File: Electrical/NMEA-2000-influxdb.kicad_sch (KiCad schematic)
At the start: 6 parts, among them U1 LM7805_TO220, U2 SN65HVD230-Module, U3 RTC-Module

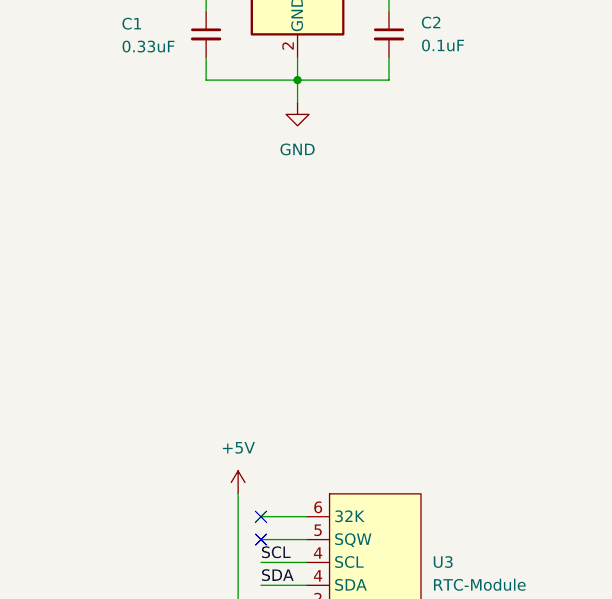
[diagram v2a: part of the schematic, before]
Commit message: Added BMP280-Module
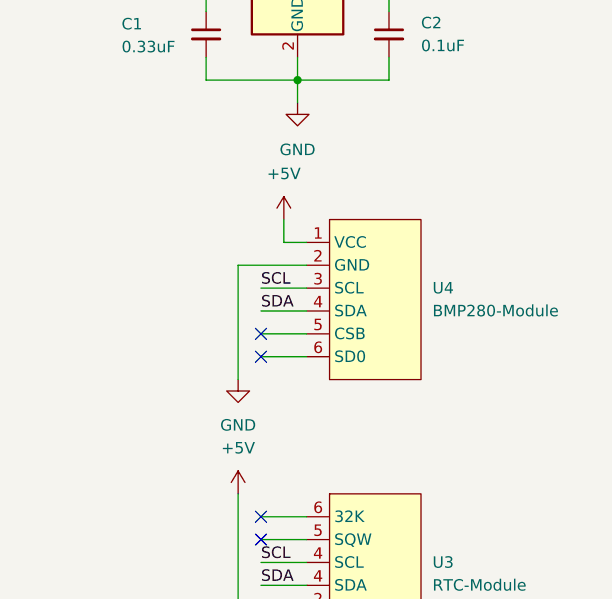
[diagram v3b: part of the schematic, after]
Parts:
- added U4: BMP280-Module, symbol BMP280-Module:BMP280-Module
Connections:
- net +5V: now also U4.1 (VCC)
- net GND: now also U4.2 (GND)
- net SCL: now also U4.3 (SCL)
- net SDA: now also U4.4 (SDA)
- no-connect marks 2 -> 4
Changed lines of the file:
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@@
   )
   (no_connect (at 222.25 99.06))
+  (no_connect (at 222.25 81.28))
   (no_connect (at 222.25 101.6))
+  (no_connect (at 222.25 78.74))
   (wire (pts (xy 222.25 99.06) (xy 227.33 99.06))
     (stroke (width 0) (type default))
   )
+  (wire (pts (xy 222.25 81.28) (xy 227.33 81.28))
+    (stroke (width 0) (type default))
+  )
+  (wire (pts (xy 222.25 76.2) (xy 227.33 76.2))
+    (stroke (width 0) (type default))
+  )
   (wire (pts (xy 222.25 109.22) (xy 222.25 114.3))
     (stroke (width 0) (type default))
@@
     (stroke (width 0) (type default))
   )
+  (wire (pts (xy 227.33 68.58) (xy 224.79 68.58))
+    (stroke (width 0) (type default))
+  )
   (wire (pts (xy 236.474 50.546) (xy 236.474 48.006))
     (stroke (width 0) (type default))
   )
+  (wire (pts (xy 219.71 71.12) (xy 227.33 71.12))
+    (stroke (width 0) (type default))
+  )
   (wire (pts (xy 210.82 137.16) (xy 210.82 144.78))
     (stroke (width 0) (type default))
@@
     (stroke (width 0) (type default))
   )
+  (wire (pts (xy 222.25 78.74) (xy 227.33 78.74))
+    (stroke (width 0) (type default))
+  )
   (wire (pts (xy 218.44 132.08) (xy 218.44 134.62))
     (stroke (width 0) (type default))
@@
     (stroke (width 0) (type default))
   )
+  (wire (pts (xy 222.25 73.66) (xy 227.33 73.66))
+    (stroke (width 0) (type default))
+  )
   (wire (pts (xy 236.474 40.386) (xy 236.474 42.926))
     (stroke (width 0) (type default))
   )
+  (wire (pts (xy 219.71 83.82) (xy 219.71 71.12))
+    (stroke (width 0) (type default))
+  )
   (wire (pts (xy 120.65 129.54) (xy 125.73 129.54))
     (stroke (width 0) (type default))
@@
     (stroke (width 0) (type default))
   )
+  (wire (pts (xy 224.79 68.58) (xy 224.79 66.04))
+    (stroke (width 0) (type default))
+  )
   (wire (pts (xy 216.154 48.006) (xy 216.154 50.546))
     (stroke (width 0) (type default))
@@
     (effects (font (size 1.27 1.27)) (justify left bottom))
   )
+  (label "SDA" (at 222.25 76.2 0) (fields_autoplaced)
+    (effects (font (size 1.27 1.27)) (justify left bottom))
+  )
   (label "CAN_RX" (at 213.36 139.7 0) (fields_autoplaced)
     (effects (font (size 1.27 1.27)) (justify left bottom))
@@
   )
   (label "SDA" (at 120.65 127 0) (fields_autoplaced)
+    (effects (font (size 1.27 1.27)) (justify left bottom))
+  )
+  (label "SCL" (at 222.25 73.66 0) (fields_autoplaced)
     (effects (font (size 1.27 1.27)) (justify left bottom))
   )
@@
         (path "/efe7a42c-525a-4afc-8476-4cc785240ca6"
           (reference "U3") (unit 1)
+        )
+      )
+    )
+  )
+  (symbol (lib_id "BMP280-Module:BMP280-Module") (at 234.95 62.23 0) (unit 1)
+    (in_bom yes) (on_board yes) (dnp no) (fields_autoplaced)
+    (property "Reference" "U4" (at 241.3 73.66 0)
+      (effects (font (size 1.27 1.27)) (justify left))
+    )
+    (property "Value" "BMP280-Module" (at 241.3 76.2 0)
+      (effects (font (size 1.27 1.27)) (justify left))
+    )
+    (property "Footprint" "" (at 234.95 62.23 0)
+      (effects (font (size 1.27 1.27)) hide)
+    )
+    (property "Datasheet" "" (at 234.95 62.23 0)
+      (effects (font (size 1.27 1.27)) hide)
+    )
+    (pin "1")
+    (pin "2")
+    (pin "3")
+    (pin "4")
+    (pin "5")
+    (pin "6")
+    (instances
+      (project "NMEA-2000-influxdb"
+        (path "/efe7a42c-525a-4afc-8476-4cc785240ca6"
+          (reference "U4") (unit 1)
         )
       )
@@
     )
   )
+  (symbol (lib_id "power:+5V") (at 224.79 66.04 0) (unit 1)
+    (in_bom yes) (on_board yes) (dnp no) (fields_autoplaced)
+    (property "Reference" "#PWR011" (at 224.79 69.85 0)
+      (effects (font (size 1.27 1.27)) hide)
+    )
+    (property "Value" "+5V" (at 224.79 60.96 0)
+      (effects (font (size 1.27 1.27)))
+    )
+    (property "Footprint" "" (at 224.79 66.04 0)
+      (effects (font (size 1.27 1.27)) hide)
+    )
+    (property "Datasheet" "" (at 224.79 66.04 0)
+      (effects (font (size 1.27 1.27)) hide)
+    )
+    (pin "1")
+    (instances
+      (project "NMEA-2000-influxdb"
+        (path "/efe7a42c-525a-4afc-8476-4cc785240ca6"
+          (reference "#PWR011") (unit 1)
+        )
+      )
+    )
+  )
   (symbol (lib_id "Regulator_Linear:LM7805_TO220") (at 226.314 40.386 0) (unit 1)
     (in_bom yes) (on_board yes) (dnp no) (fields_autoplaced)
@@
         )
       )
+    )
+  )
+  (symbol (lib_id "power:GND") (at 219.71 83.82 0) (unit 1)
+    (in_bom yes) (on_board yes) (dnp no) (fields_autoplaced)
+    (property "Reference" "#PWR012" (at 219.71 90.17 0)
+      (effects (font (size 1.27 1.27)) hide)
+    )
+    (property "Value" "GND" (at 219.71 88.9 0)
+      (effects (font (size 1.27 1.27)))
+    )
+    (property "Footprint" "" (at 219.71 83.82 0)
+      (effects (font (size 1.27 1.27)) hide)
+    )
+    (property "Datasheet" "" (at 219.71 83.82 0)
+      (effects (font (size 1.27 1.27)) hide)
+    )
+    (pin "1")
+    (instances
+      (project "NMEA-2000-influxdb"
+        (path "/efe7a42c-525a-4afc-8476-4cc785240ca6"
+          (reference "#PWR012") (unit 1)
+        )
+      )

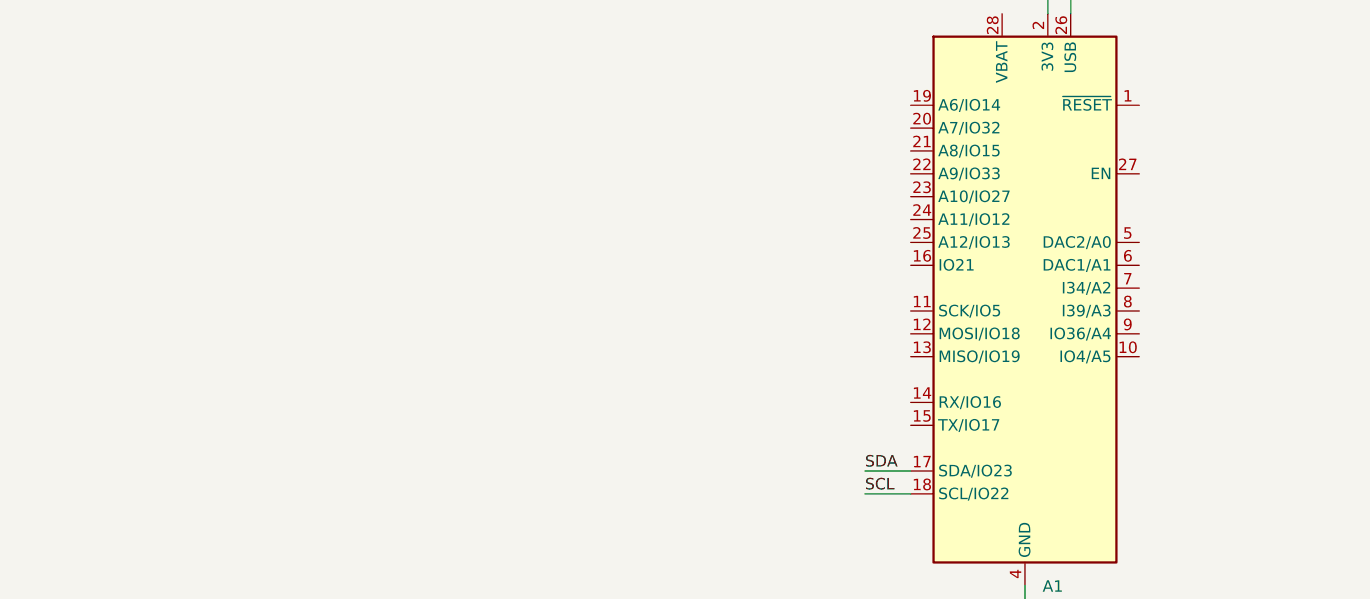
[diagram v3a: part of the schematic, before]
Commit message: Added SD-Card-Module to Schematic
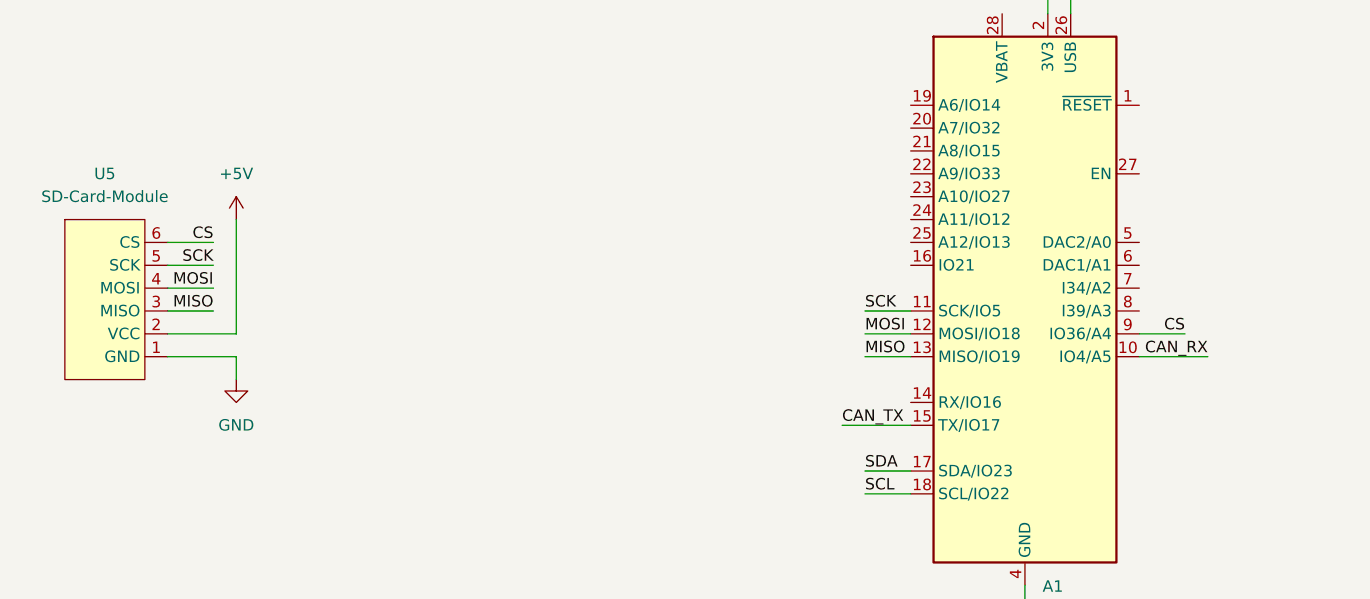
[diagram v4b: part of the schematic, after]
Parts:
- added U5: SD-Card-Module, symbol SD-Card-Module:SD-Card-Module
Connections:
- net +5V: now also U5.2 (VCC)
- net CAN_RX: now also A1.10 (IO4/A5)
- net CAN_TX: now also A1.15 (TX/IO17)
- net GND: now also U5.1 (GND)
- net SCK: now reaches A1.11 (SCK/IO5)
- net SCK: now also U5.5 (SCK)
- net MOSI: now reaches A1.12 (MOSI/IO18)
- net MOSI: now also U5.4 (MOSI)
- net MISO: now reaches A1.13 (MISO/IO19)
- net MISO: now also U5.3 (MISO)
- net CS: now reaches A1.9 (IO36/A4)
- net CS: now also U5.6 (CS)
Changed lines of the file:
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@@
   (no_connect (at 222.25 101.6))
   (no_connect (at 222.25 78.74))
+  (wire (pts (xy 125.73 111.76) (xy 120.65 111.76))
+    (stroke (width 0) (type default))
+  )
   (wire (pts (xy 222.25 99.06) (xy 227.33 99.06))
     (stroke (width 0) (type default))
@@
     (stroke (width 0) (type default))
   )
+  (wire (pts (xy 151.13 111.76) (xy 156.21 111.76))
+    (stroke (width 0) (type default))
+  )
+  (wire (pts (xy 50.8 99.06) (xy 50.8 111.76))
+    (stroke (width 0) (type default))
+  )
   (wire (pts (xy 222.25 109.22) (xy 222.25 114.3))
     (stroke (width 0) (type default))
@@
     (stroke (width 0) (type default))
   )
+  (wire (pts (xy 43.18 101.6) (xy 48.26 101.6))
+    (stroke (width 0) (type default))
+  )
   (wire (pts (xy 140.97 73.66) (xy 140.97 76.2))
     (stroke (width 0) (type default))
@@
     (stroke (width 0) (type default))
   )
+  (wire (pts (xy 43.18 114.3) (xy 50.8 114.3))
+    (stroke (width 0) (type default))
+  )
   (wire (pts (xy 210.82 137.16) (xy 210.82 144.78))
     (stroke (width 0) (type default))
@@
     (stroke (width 0) (type default))
   )
+  (wire (pts (xy 125.73 114.3) (xy 120.65 114.3))
+    (stroke (width 0) (type default))
+  )
   (wire (pts (xy 218.44 132.08) (xy 218.44 134.62))
     (stroke (width 0) (type default))
@@
     (stroke (width 0) (type default))
   )
+  (wire (pts (xy 43.18 104.14) (xy 48.26 104.14))
+    (stroke (width 0) (type default))
+  )
   (wire (pts (xy 120.65 127) (xy 125.73 127))
     (stroke (width 0) (type default))
@@
     (stroke (width 0) (type default))
   )
+  (wire (pts (xy 50.8 111.76) (xy 43.18 111.76))
+    (stroke (width 0) (type default))
+  )
   (wire (pts (xy 236.474 40.386) (xy 236.474 42.926))
     (stroke (width 0) (type default))
   )
+  (wire (pts (xy 43.18 109.22) (xy 48.26 109.22))
+    (stroke (width 0) (type default))
+  )
   (wire (pts (xy 219.71 83.82) (xy 219.71 71.12))
     (stroke (width 0) (type default))
@@
     (stroke (width 0) (type default))
   )
+  (wire (pts (xy 125.73 109.22) (xy 120.65 109.22))
+    (stroke (width 0) (type default))
+  )
   (wire (pts (xy 222.25 104.14) (xy 227.33 104.14))
     (stroke (width 0) (type default))
   )
+  (wire (pts (xy 118.11 121.92) (xy 125.73 121.92))
+    (stroke (width 0) (type default))
+  )
   (wire (pts (xy 219.71 96.52) (xy 219.71 111.76))
     (stroke (width 0) (type default))
@@
     (stroke (width 0) (type default))
   )
+  (wire (pts (xy 158.75 114.3) (xy 151.13 114.3))
+    (stroke (width 0) (type default))
+  )
   (wire (pts (xy 216.154 48.006) (xy 216.154 50.546))
     (stroke (width 0) (type default))
@@
     (stroke (width 0) (type default))
   )
+  (wire (pts (xy 43.18 106.68) (xy 48.26 106.68))
+    (stroke (width 0) (type default))
+  )
+  (wire (pts (xy 50.8 114.3) (xy 50.8 116.84))
+    (stroke (width 0) (type default))
+  )
   (wire (pts (xy 216.154 37.846) (xy 216.154 40.386))
     (stroke (width 0) (type default))
@@
     (effects (font (size 1.27 1.27)) (justify left bottom))
   )
+  (label "CAN_RX" (at 158.75 114.3 180) (fields_autoplaced)
+    (effects (font (size 1.27 1.27)) (justify right bottom))
+  )
+  (label "MISO" (at 120.65 114.3 0) (fields_autoplaced)
+    (effects (font (size 1.27 1.27)) (justify left bottom))
+  )
+  (label "CS" (at 156.21 111.76 180) (fields_autoplaced)
+    (effects (font (size 1.27 1.27)) (justify right bottom))
+  )
+  (label "SCK" (at 48.26 104.14 180) (fields_autoplaced)
+    (effects (font (size 1.27 1.27)) (justify right bottom))
+  )
+  (label "MOSI" (at 48.26 106.68 180) (fields_autoplaced)
+    (effects (font (size 1.27 1.27)) (justify right bottom))
+  )
+  (label "SCK" (at 120.65 109.22 0) (fields_autoplaced)
+    (effects (font (size 1.27 1.27)) (justify left bottom))
+  )
+  (label "MISO" (at 48.26 109.22 180) (fields_autoplaced)
+    (effects (font (size 1.27 1.27)) (justify right bottom))
+  )
   (label "CAN_RX" (at 213.36 139.7 0) (fields_autoplaced)
     (effects (font (size 1.27 1.27)) (justify left bottom))
   )
+  (label "MOSI" (at 120.65 111.76 0) (fields_autoplaced)
+    (effects (font (size 1.27 1.27)) (justify left bottom))
+  )
   (label "SCL" (at 222.25 104.14 0) (fields_autoplaced)
     (effects (font (size 1.27 1.27)) (justify left bottom))
@@
     (effects (font (size 1.27 1.27)) (justify left bottom))
   )
+  (label "CAN_TX" (at 118.11 121.92 0) (fields_autoplaced)
+    (effects (font (size 1.27 1.27)) (justify left bottom))
+  )
   (label "SCL" (at 222.25 73.66 0) (fields_autoplaced)
     (effects (font (size 1.27 1.27)) (justify left bottom))
@@
   (label "CAN_TX" (at 213.36 142.24 0) (fields_autoplaced)
     (effects (font (size 1.27 1.27)) (justify left bottom))
+  )
+  (label "CS" (at 48.26 101.6 180) (fields_autoplaced)
+    (effects (font (size 1.27 1.27)) (justify right bottom))
   )
   (global_label "CAN_L" (shape input) (at 248.92 137.16 0) (fields_autoplaced)
@@
         )
       )
+    )
+  )
+  (symbol (lib_id "power:+5V") (at 50.8 99.06 0) (unit 1)
+    (in_bom yes) (on_board yes) (dnp no) (fields_autoplaced)
+    (property "Reference" "#PWR014" (at 50.8 102.87 0)
+      (effects (font (size 1.27 1.27)) hide)
+    )
+    (property "Value" "+5V" (at 50.8 93.98 0)
+      (effects (font (size 1.27 1.27)))
+    )
+    (property "Footprint" "" (at 50.8 99.06 0)
+      (effects (font (size 1.27 1.27)) hide)
+    )
+    (property "Datasheet" "" (at 50.8 99.06 0)
+      (effects (font (size 1.27 1.27)) hide)
+    )
+    (pin "1")
+    (instances
+      (project "NMEA-2000-influxdb"
+        (path "/efe7a42c-525a-4afc-8476-4cc785240ca6"
+          (reference "#PWR014") (unit 1)
+        )
+      )
+    )
+  )
+  (symbol (lib_id "power:GND") (at 50.8 116.84 0) (unit 1)
+    (in_bom yes) (on_board yes) (dnp no) (fields_autoplaced)
+    (property "Reference" "#PWR013" (at 50.8 123.19 0)
+      (effects (font (size 1.27 1.27)) hide)
+    )
+    (property "Value" "GND" (at 50.8 121.92 0)
+      (effects (font (size 1.27 1.27)))
+    )
+    (property "Footprint" "" (at 50.8 116.84 0)
+      (effects (font (size 1.27 1.27)) hide)
+    )
+    (property "Datasheet" "" (at 50.8 116.84 0)
+      (effects (font (size 1.27 1.27)) hide)
+    )
+    (pin "1")
+    (instances
+      (project "NMEA-2000-influxdb"
+        (path "/efe7a42c-525a-4afc-8476-4cc785240ca6"
+          (reference "#PWR013") (unit 1)
+        )
+      )
+    )
+  )
+  (symbol (lib_id "SD-Card-Module:SD-Card-Module") (at 35.56 93.98 0) (unit 1)
+    (in_bom yes) (on_board yes) (dnp no) (fields_autoplaced)
+    (property "Reference" "U5" (at 36.195 93.98 0)
+      (effects (font (size 1.27 1.27)))
+    )
+    (property "Value" "SD-Card-Module" (at 36.195 96.52 0)
+      (effects (font (size 1.27 1.27)))
+    )
+    (property "Footprint" "" (at 35.56 93.98 0)
+      (effects (font (size 1.27 1.27)) hide)
+    )
+    (property "Datasheet" "" (at 35.56 93.98 0)
+      (effects (font (size 1.27 1.27)) hide)
+    )
+    (pin "1")
+    (pin "2")
+    (pin "3")
+    (pin "4")
+    (pin "5")
+    (pin "6")
+    (instances
+      (project "NMEA-2000-influxdb"
+        (path "/efe7a42c-525a-4afc-8476-4cc785240ca6"
+          (reference "U5") (unit 1)
+        )
+      )
